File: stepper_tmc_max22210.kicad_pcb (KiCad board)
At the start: 4 copper layers, 15.2 x 20.3 mm, 3 parts, among them J1 Conn_01x08_pin, J2 Conn_01x08_pin, U1 MAX22210ATJ+

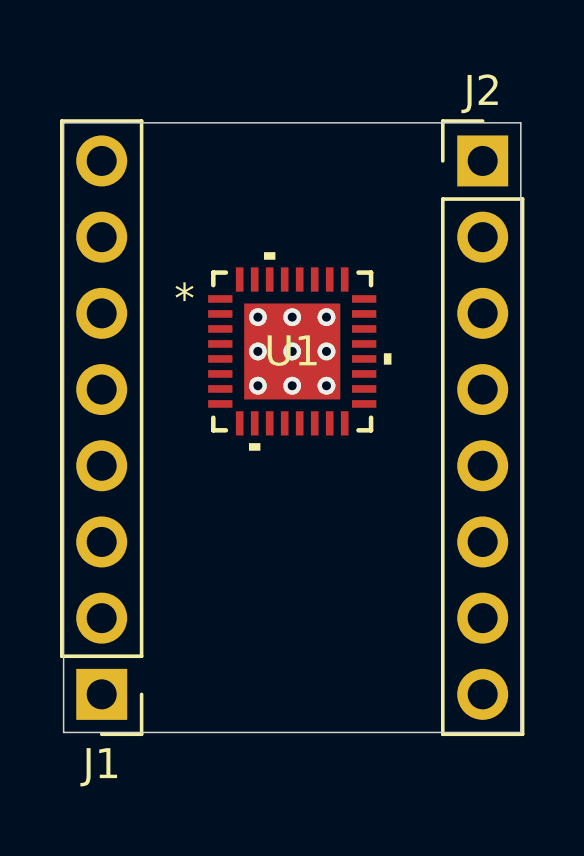
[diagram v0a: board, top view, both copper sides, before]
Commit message: Finished functional design, ready for silk screen and BOM revision
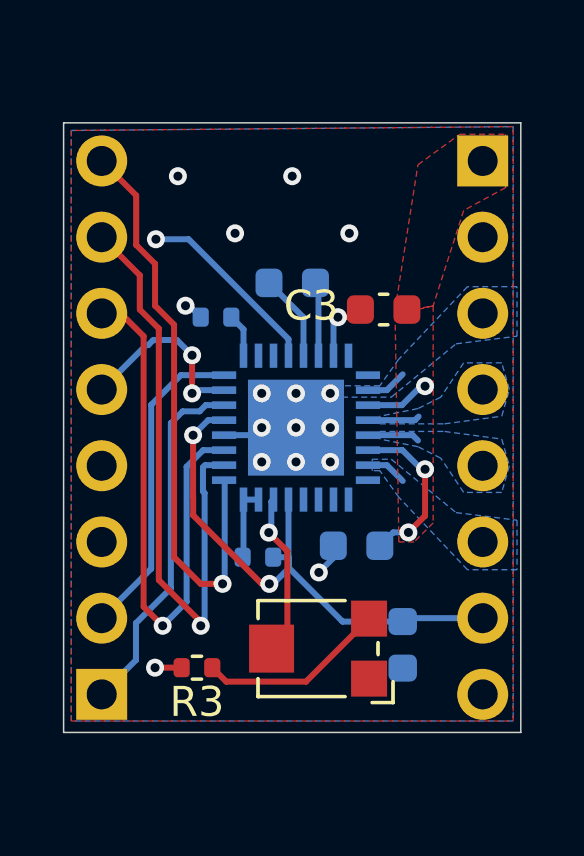
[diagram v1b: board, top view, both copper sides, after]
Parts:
- added 50k1: rot_pot, Potentiometer_SMD:Potentiometer_Bourns_TC33X_Vertical, F.Cu at (145.5, 104.6)
- added C1: 22nF, Capacitor_SMD:C_0603_1608Metric, B.Cu at (144.8, 92.5)
- added C3: 1uf, Capacitor_SMD:C_0603_1608Metric, F.Cu at (147.8, 93.3)
- added C6: 1uF, Capacitor_SMD:C_0603_1608Metric, B.Cu at (146.9, 101.2)
- added C7: 1uf, Capacitor_SMD:C_0603_1608Metric, B.Cu at (148.5, 104.5)
- added R1: 10k, Resistor_SMD:R_0402_1005Metric, B.Cu at (142.2, 93.6)
- added R2: 10k, Resistor_SMD:R_0402_1005Metric, B.Cu at (143.6, 101.6)
- added R3: 12k, Resistor_SMD:R_0402_1005Metric, F.Cu at (141.6, 105.3)
- J1, J2, U1: moved to B.Cu
- moved U1 2.54 mm to (144.9, 97.3)
- turned J1 to 0 degrees
- turned J2 to 180 degrees
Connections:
- J1 pad 1: unconnected-(J1-Pin_1-Pad1) -> DIR
- J1 pad 2: unconnected-(J1-Pin_2-Pad2) -> STEP
- J1 pad 3: unconnected-(J1-Pin_3-Pad3) -> SLEEP
- J1 pad 4: unconnected-(J1-Pin_4-Pad4) -> SLEEP
- J1 pad 5: unconnected-(J1-Pin_5-Pad5) -> MODE2
- J1 pad 6: unconnected-(J1-Pin_6-Pad6) -> MODE1
- J1 pad 7: unconnected-(J1-Pin_7-Pad7) -> MODE0
- J2 pad 1: unconnected-(J2-Pin_1-Pad1) -> VMOT
- J2 pad 2: unconnected-(J2-Pin_2-Pad2) -> GND
- J2 pad 3: unconnected-(J2-Pin_3-Pad3) -> M2
- J2 pad 4: unconnected-(J2-Pin_4-Pad4) -> M1
- J2 pad 5: unconnected-(J2-Pin_5-Pad5) -> M3
- J2 pad 6: unconnected-(J2-Pin_6-Pad6) -> M4
- J2 pad 7: unconnected-(J2-Pin_7-Pad7) -> VDD
- J2 pad 8: unconnected-(J2-Pin_8-Pad8) -> GND
- U1 pad 1: unconnected-(U1-EN-Pad1) -> EN
- U1 pad 12: unconnected-(U1-SLEEP-Pad12) -> SLEEP
- U1 pad 13: unconnected-(U1-CP2-Pad13) -> Net-(U1-CP2)
- U1 pad 14: unconnected-(U1-CP1-Pad14) -> Net-(U1-CP1)
- U1 pad 15: unconnected-(U1-VCP-Pad15) -> Net-(U1-VCP)
- U1 pad 18: unconnected-(U1-OUT1B-Pad18) -> M2
- U1 pad 19: unconnected-(U1-VM-Pad19) -> VMOT
- U1 pad 2: unconnected-(U1-MODE0-Pad2) -> MODE0
- U1 pad 20: unconnected-(U1-OUT2B-Pad20) -> M1
- U1 pad 21: unconnected-(U1-OUT2A-Pad21) -> M3
- U1 pad 22: unconnected-(U1-VM-Pad22) -> VMOT
- U1 pad 23: unconnected-(U1-OUT1A-Pad23) -> M4
- U1 pad 29: unconnected-(U1-ROFF-Pad29) -> VDD
- U1 pad 3: unconnected-(U1-MODE1-Pad3) -> MODE1
- U1 pad 30: unconnected-(U1-REF-Pad30) -> Net-(U1-REF)
- U1 pad 31: unconnected-(U1-DECAY2-Pad31) -> Net-(U1-DECAY1)
- U1 pad 32: unconnected-(U1-DECAY1-Pad32) -> Net-(U1-DECAY1)
- U1 pad 33: unconnected-(U1-EPAD-Pad33) -> GND
- U1 pad 4: unconnected-(U1-AGND-Pad4) -> GND
- U1 pad 5: unconnected-(U1-VDD-Pad5) -> VDD
- U1 pad 6: unconnected-(U1-DIR-Pad6) -> DIR
- U1 pad 7: unconnected-(U1-MODE2-Pad7) -> MODE2
- U1 pad 8: unconnected-(U1-STEP-Pad8) -> STEP
- U1 pad 9: unconnected-(U1-HFS-Pad9) -> hfs_select
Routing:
- net MODE0: track 0.00 -> 20.4 mm, vias 0 -> 1
- net EN: track 0.00 -> 19.7 mm, vias 0 -> 1
- net MODE1: track 0.00 -> 18.7 mm, vias 0 -> 1
- net VDD: track 0.00 -> 18.7 mm, vias 0 -> 2
- net SLEEP: track 0.00 -> 17.2 mm, vias 0 -> 1
- net DIR: track 0.00 -> 12.0 mm
- net STEP: track 0.00 -> 10.6 mm
- net VMOT: track 0.00 -> 7.80 mm, vias 0 -> 3
- net Net-(50k1-Pad3): track 0.00 -> 6.29 mm
- net MODE2: track 0.00 -> 6.29 mm, vias 0 -> 2
- net Net-(U1-REF): track 0.00 -> 5.51 mm, vias 0 -> 1
- net GND: track 0.00 -> 4.00 mm, vias 0 -> 16
- net Net-(U1-CP2): track 0.00 -> 2.92 mm
- net Net-(U1-CP1): track 0.00 -> 2.47 mm
- net Net-(U1-DECAY1): track 0.00 -> 2.43 mm
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- added copper zone on B.Cu, net GND
- added copper zone on F.Cu, net GND
- added copper zone on In1.Cu, net GND
- added copper zone on In2.Cu, net GND
- added copper zone on B.Cu, net M1
- added copper zone on B.Cu, net M2
- added copper zone on B.Cu, net M3
- added copper zone on B.Cu, net M4
- added copper zone on F.Cu, net VMOT

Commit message: small pcb adjustments for photos
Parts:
- C3: moved to B.Cu
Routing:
- net VDD: track 18.7 -> 23.3 mm
- net VMOT: track 7.80 -> 8.90 mm, vias 3 -> 4
- net Net-(U1-VCP): track 2.20 -> 1.91 mm, vias 1 -> 0
